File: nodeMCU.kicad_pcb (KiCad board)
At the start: 2 copper layers, 25.4 x 48.3 mm, 38 parts, among them J1 USB_B_Micro, J2 Conn_01x15, J3 Conn_01x15, Q1 S8050, Q2 S8050, SW1 RESET, SW2 FLASH, U1 AP1117-33, U2 CP2102N-A01-GQFN28, U3 ESP-12E

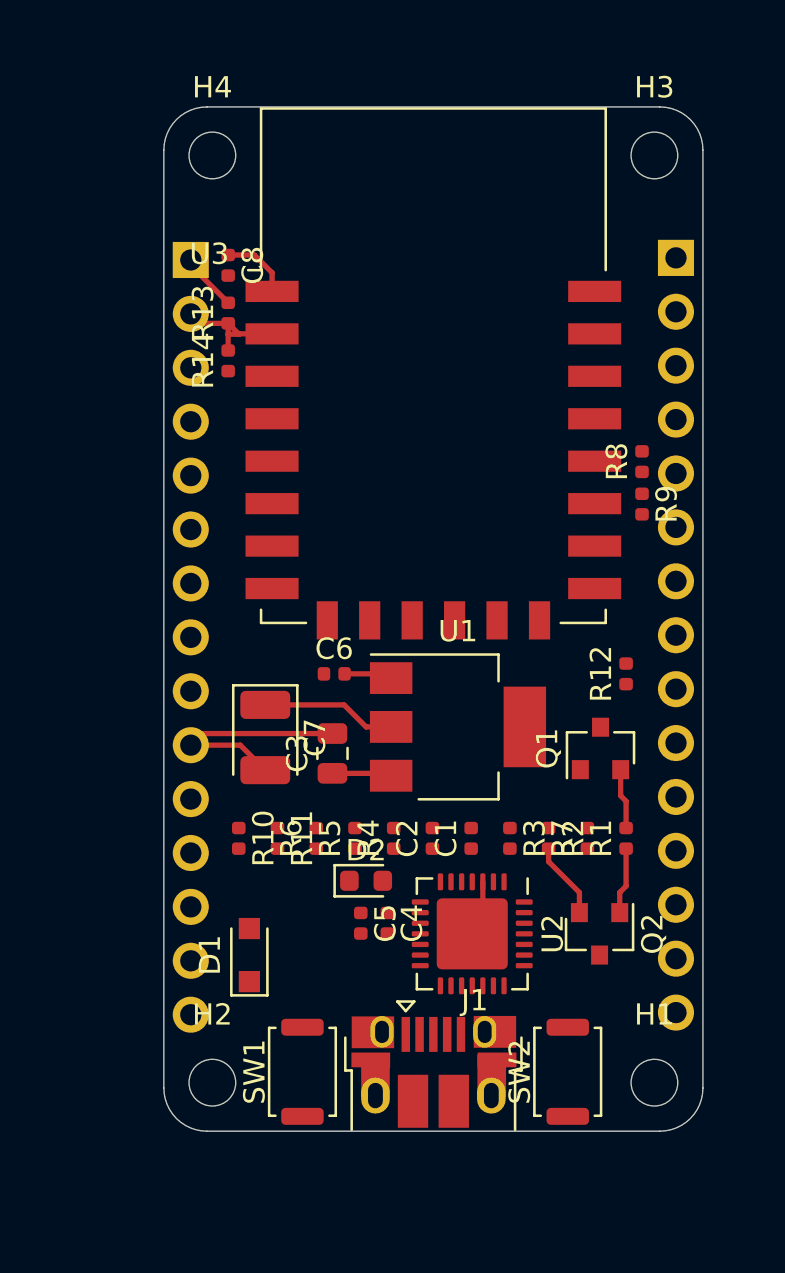
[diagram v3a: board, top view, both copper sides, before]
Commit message: Cambios propuesto por el docente en el esquematico
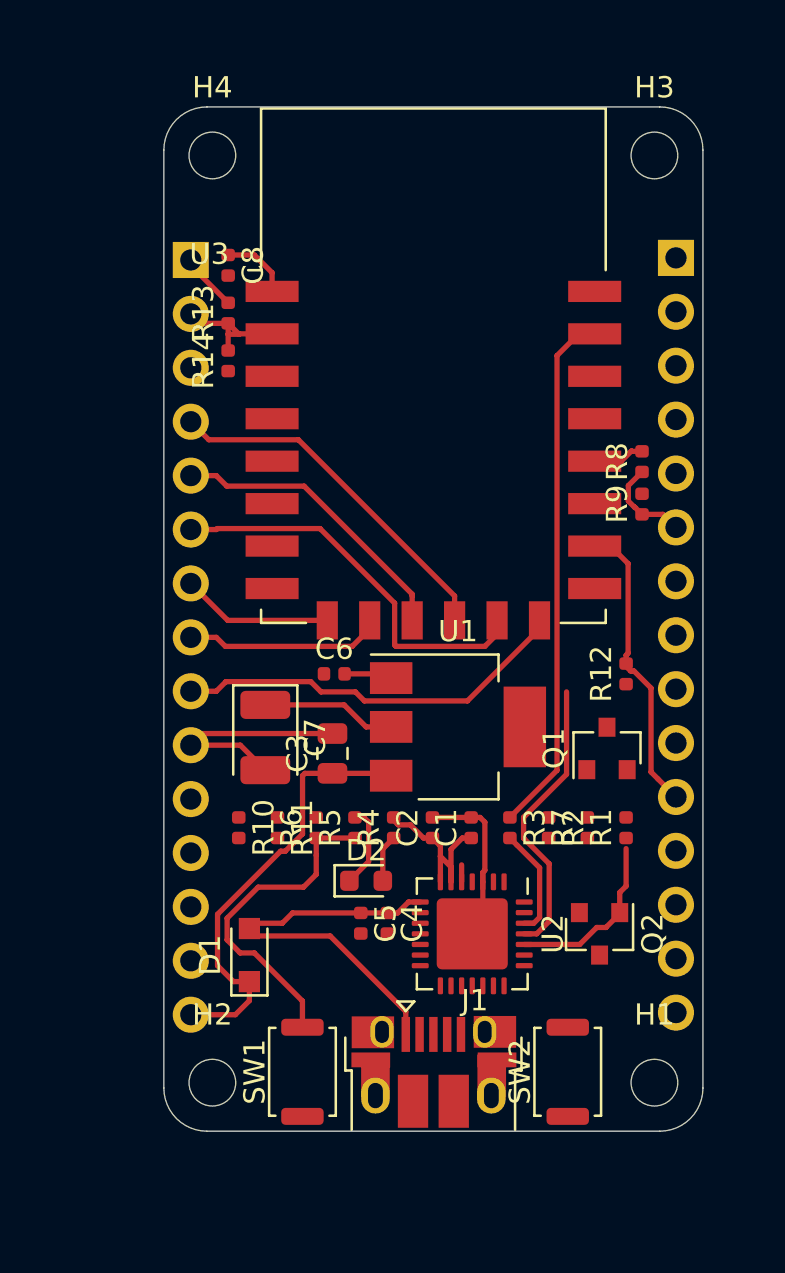
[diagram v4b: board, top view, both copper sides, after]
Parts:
- moved C1 0.50 mm to (187.2, 84.0)
- moved C2 0.50 mm to (185.4, 84.0)
- moved R1 0.50 mm to (194.5, 84.0)
- moved R10 0.50 mm to (176.2, 84.0)
- moved R11 0.50 mm to (178.1, 84.0)
- moved R2 0.50 mm to (190.8, 84.0)
- moved R3 0.50 mm to (189.0, 84.0)
- moved R4 0.50 mm to (183.6, 84.0)
- moved R5 0.50 mm to (181.7, 84.0)
- moved R6 0.50 mm to (179.9, 84.0)
- moved R7 0.50 mm to (192.7, 84.0)
- moved Q1 0.31 mm to (193.6, 80.3)
- turned R9 to 90 degrees
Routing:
- net /RXD: track 0.00 -> 24.9 mm
- net /SCLK: track 0.00 -> 18.8 mm
- net /MOSI: track 0.00 -> 18.8 mm
- net VBUS: track 0.00 -> 18.6 mm
- net +5V: track 2.81 -> 20.8 mm
- net /GPIO_10: track 0.00 -> 17.0 mm
- net Net-(R5-Pad1): track 0.00 -> 15.6 mm
- net /GPIO_15: track 0.00 -> 14.0 mm
- net /GPIO_9: track 0.00 -> 14.0 mm
- net /TXD: track 0.00 -> 13.6 mm
- net +3V3: track 6.36 -> 19.4 mm
- net /MISO: track 0.00 -> 9.35 mm
- net /CS0: track 0.00 -> 7.15 mm
- net GND: track 15.8 -> 21.2 mm
- net Net-(R3-Pad2): track 0.00 -> 5.16 mm
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
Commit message: Borro ruteo
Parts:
- J1: footprint Connector_USB:USB_Micro-B_Amphenol_10103594-0001LF_Horizontal -> Connector_USB:USB_Micro-B_Molex-105017-0001
- moved H1 1.60 mm to (195.8, 97.6)
- moved H2 1.60 mm to (175.0, 97.6)
- moved J1 1.60 mm to (185.4, 97.1)
- moved SW1 1.60 mm to (179.2, 97.1)
- moved SW2 1.60 mm to (191.8, 97.1)
- moved D1 1.56 mm to (177.8, 91.1), turned to 0 degrees
- moved C4 0.73 mm to (183.1, 89.2)
- moved Q2 0.73 mm to (193.1, 89.7)
- moved U2 0.73 mm to (187.1, 89.7)
- moved C5 0.70 mm to (182.0, 89.2)
- moved R12 0.59 mm to (194.1, 77.2), turned to 0 degrees
- moved C3 0.29 mm to (180.9, 80.5)
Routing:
- net /nRST: track 3.30 -> 72.6 mm, vias 0 -> 1
- net /TXD: track 13.6 -> 46.5 mm, vias 0 -> 1
- net +3V3: track 19.4 -> 47.9 mm
- net /EN: track 0.00 -> 28.5 mm, vias 0 -> 2
- net /GPIO_0: track 2.44 -> 26.3 mm
- net /GPIO_14: track 0.00 -> 22.6 mm, vias 0 -> 1
- net /GPIO_16: track 3.87 -> 26.0 mm
- net Net-(J1-Pad3): track 0.00 -> 11.3 mm, vias 0 -> 2
- net Net-(J1-Pad2): track 0.80 -> 11.3 mm, vias 0 -> 1
- net /RXD: track 24.9 -> 34.7 mm, vias 0 -> 1
- net /nDTR_CP: track 0.00 -> 9.53 mm, vias 0 -> 2
- net /SCLK: track 18.8 -> 25.3 mm
- net /MISO: track 9.35 -> 14.7 mm
- net /GPIO_5: track 0.00 -> 5.09 mm
- net Net-(Q2-Pad2): track 0.00 -> 4.98 mm
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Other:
- board size 25.4 x 48.3 mm -> 25.4 x 50 mm
- net class Default: clearance 0.2 -> 0.1
- rule trace_clearance: 0.2 -> 0.1
- rule trace_min: 0.2 -> 0.15
- rule via_min_drill: 0.3 -> 0.15
- rule via_min_size: 0.4 -> 0.2

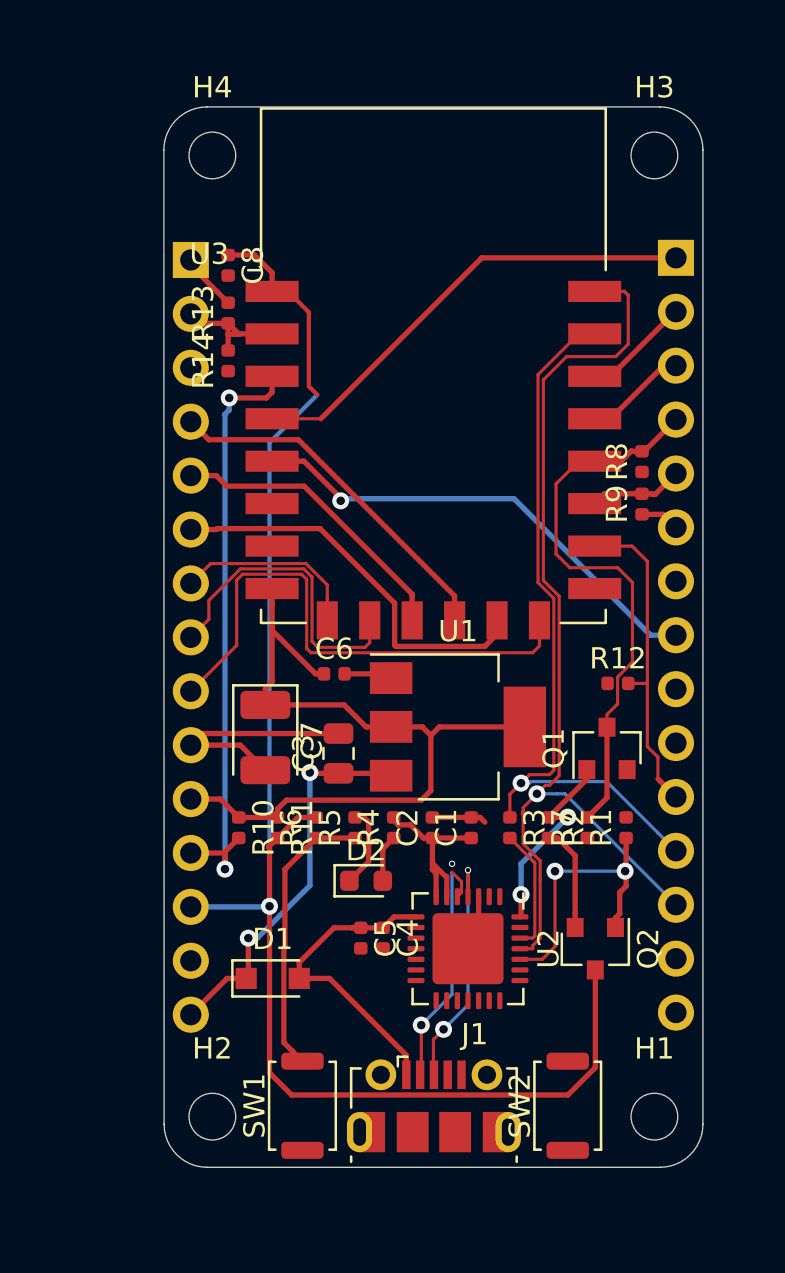
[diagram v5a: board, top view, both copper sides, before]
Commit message: Termino el ruteo
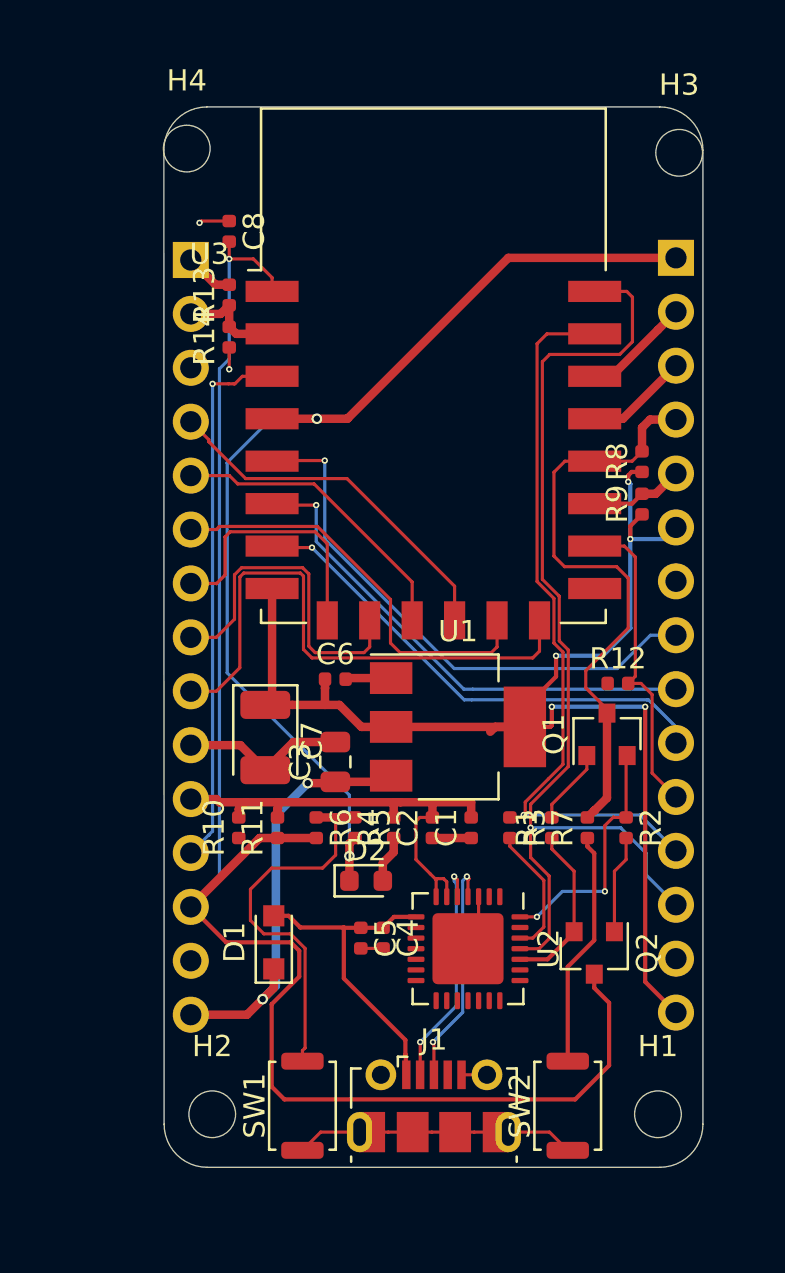
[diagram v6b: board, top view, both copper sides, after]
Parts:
- moved R2 3.65 mm to (194.5, 84.0)
- moved R1 3.50 mm to (191.0, 84.0)
- moved D1 1.70 mm to (177.9, 89.4), turned to 90 degrees
- moved C8 1.60 mm to (175.8, 55.9)
- moved H4 1.25 mm to (173.8, 52.0)
- moved H3 1.17 mm to (197.0, 52.2)
- moved R14 1.12 mm to (175.8, 60.9)
- moved R13 0.85 mm to (175.8, 58.9)
- moved Q1 0.66 mm to (193.6, 79.6)
- moved C3 0.43 mm to (180.8, 80.9)
- moved C6 0.25 mm to (180.8, 77.0)
- moved Q2 0.21 mm to (193.0, 89.9)
- moved H1 0.20 mm to (196.0, 97.5)
- moved H2 0.11 mm to (175.0, 97.5)
- turned R10 to 90 degrees
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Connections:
- C1 pad 1: +3V3 -> GND
- C1 pad 2: GND -> +3V3
- C2 pad 1: +3V3 -> GND
- C2 pad 2: GND -> +3V3
- C8 pad 1: /nRST -> GND
- C8 pad 2: GND -> /nRST
- Q1 pad 1: /nDTR_CP -> Net-(Q1-Pad1)
- Q1 pad 2: Net-(Q1-Pad2) -> /nDTR_CP
- Q2 pad 1: /nRTS_CP -> Net-(Q2-Pad1)
- Q2 pad 2: Net-(Q2-Pad2) -> /nRTS_CP
- R1 pad 2: Net-(Q1-Pad2) -> Net-(Q1-Pad1)
- R10 pad 1: +3V3 -> /EN
- R10 pad 2: /EN -> +3V3
- R11 pad 1: +3V3 -> /nRST
- R11 pad 2: /nRST -> +3V3
- R2 pad 2: Net-(Q2-Pad2) -> Net-(Q2-Pad1)
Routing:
- net +3V3: track 47.9 -> 85.6 mm, vias 0 -> 5
- net /GPIO_16: track 26.0 -> 50.3 mm, vias 0 -> 2
- net /GPIO_12: track 0.00 -> 23.7 mm, vias 0 -> 1
- net /GPIO_13: track 0.00 -> 23.3 mm, vias 0 -> 1
- net GND: track 18.4 -> 32.9 mm, vias 0 -> 2
- net Net-(R7-Pad1): track 0.00 -> 11.2 mm
- net /nRTS_CP: track 13.2 -> 7.97 mm, vias 2 -> 0
- net Net-(Q2-Pad2): track 4.98 -> 0.00 mm
- net Net-(R5-Pad1): track 13.3 -> 18.2 mm
- net Net-(Q2-Pad1): track 0.00 -> 4.64 mm
- net /nRST: track 72.6 -> 76.7 mm
- net Net-(Q1-Pad1): track 0.00 -> 3.60 mm
- net /CS0: track 8.90 -> 12.3 mm
- net /GPIO_14: track 22.6 -> 25.9 mm
- net /EN: track 28.5 -> 25.5 mm, vias 2 -> 1
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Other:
- rule via_min_size: 0.2 -> 0.15

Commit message: Agregp logos
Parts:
- added REF**: OSHW-Symbol_6.7x6mm_SilkScreen, Symbol:OSHW-Symbol_6.7x6mm_SilkScreen, B.Cu at (185.4, 55.6)
- added REF**: KiCad-Logo2_5mm_SilkScreen, Symbol:KiCad-Logo2_5mm_SilkScreen, B.Cu at (185.4, 72.6)
- moved J2 0.74 mm to (173.2, 57.2)
- moved J3 0.65 mm to (197.5, 57.1)
- moved C8 0.50 mm to (175.8, 55.4)
- moved H1 0.50 mm to (196.5, 97.5)
- moved H2 0.40 mm to (174.6, 97.5)
- renumbered SW2 to FLASH, SW1 to RESET
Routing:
- net GND: track 32.9 -> 45.0 mm, vias 2 -> 13
- net /GPIO_10: track 17.3 -> 20.4 mm
- net /EN: track 25.5 -> 28.1 mm
- net /nRST: track 76.7 -> 74.7 mm
- net /GPIO_9: track 14.3 -> 15.4 mm
- net /CS0: track 12.3 -> 13.4 mm
- net /MOSI: track 19.5 -> 20.5 mm
- net /ADC_EX: track 2.29 -> 3.03 mm
- added copper zone on F.Cu, net +3V3
- added copper zone on F.Cu, net VBUS
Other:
- board size 25.4 x 50 mm -> 27 x 50 mm
- board text added: "+3V3"
- board text added: "+5V"
- board text added: "3.3v"
- board text added: "A0"
- board text added: "ADC0"
- board text added: "CLK"
- board text added: "CS"
- board text added: "CS0"
- board text added: "D0"
- board text added: "D1"
- board text added: "D2"
- board text added: "D3"
- board text added: "D4"
- board text added: "D5"
- board text added: "D6"
- board text added: "D7"
- board text added: "D8"
- board text added: "EN"
- board text added: "GND"
- board text added: "GPIO_0"
- board text added: "GPIO_10"
- board text added: "GPIO_12"
- board text added: "GPIO_13"
- board text added: "GPIO_14"
- board text added: "GPIO_15"
- board text added: "GPIO_16"
- board text added: "GPIO_2"
- board text added: "GPIO_4"
- board text added: "GPIO_5"
- board text added: "GPIO_9"
- board text added: "HECHO EN ARGENTINA"
- board text added: "MISO"
- board text added: "MOSI"
- board text added: "REPLICA NodeMCU kit v1.0"
- board text added: "RST"
- board text added: "RSV"
- board text added: "RXD"
- board text added: "S1"
- board text added: "S2"
- board text added: "SCLK"
- board text added: "TXD"
- board text added: "VIN"

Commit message: Agrego bvistas 3ds
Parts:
- moved REF** 4.83 mm to (183.4, 60.0)
- moved REF** 3.31 mm to (183.4, 75.2)
- moved H4 2.01 mm to (171.8, 51.8)
- moved C1 2.00 mm to (185.2, 84.0)
- moved C2 2.00 mm to (183.4, 84.0)
- moved C3 2.00 mm to (178.8, 80.9)
- moved C4 2.00 mm to (181.1, 89.2)
- moved C5 2.00 mm to (180.0, 89.2)
- moved C6 2.00 mm to (178.8, 77.0)
- moved C7 2.00 mm to (175.5, 79.8)
- moved C8 2.00 mm to (173.8, 55.4)
- moved D1 2.00 mm to (175.9, 89.4)
- moved D2 2.00 mm to (180.2, 86.5)
- moved FLASH 2.00 mm to (189.8, 97.1)
- moved H1 2.00 mm to (194.5, 97.5)
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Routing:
- net GND: track 45.0 -> 62.8 mm, vias 13 -> 106
- net /nRST: track 74.7 -> 77.2 mm
- net /GPIO_14: track 25.9 -> 23.8 mm
- net +3V3: track 85.6 -> 84.3 mm
- net /GPIO_15: track 14.9 -> 15.8 mm
- net /GPIO_0: track 29.0 -> 28.4 mm
- added copper zone on B.Cu, net GND
- added copper zone on F.Cu, net GND
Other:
- outline, holes or cut-outs redrawn
